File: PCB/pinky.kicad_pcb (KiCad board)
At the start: 2 copper layers, 134.3 x 87.6 mm, 50 parts, among them SW10 Switch, SW11 Switch, SW12 Switch, SW13 Switch, SW14 Switch, SW15 Switch, SW16 Switch, SW17 Switch, SW18 Switch, SW2 Switch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

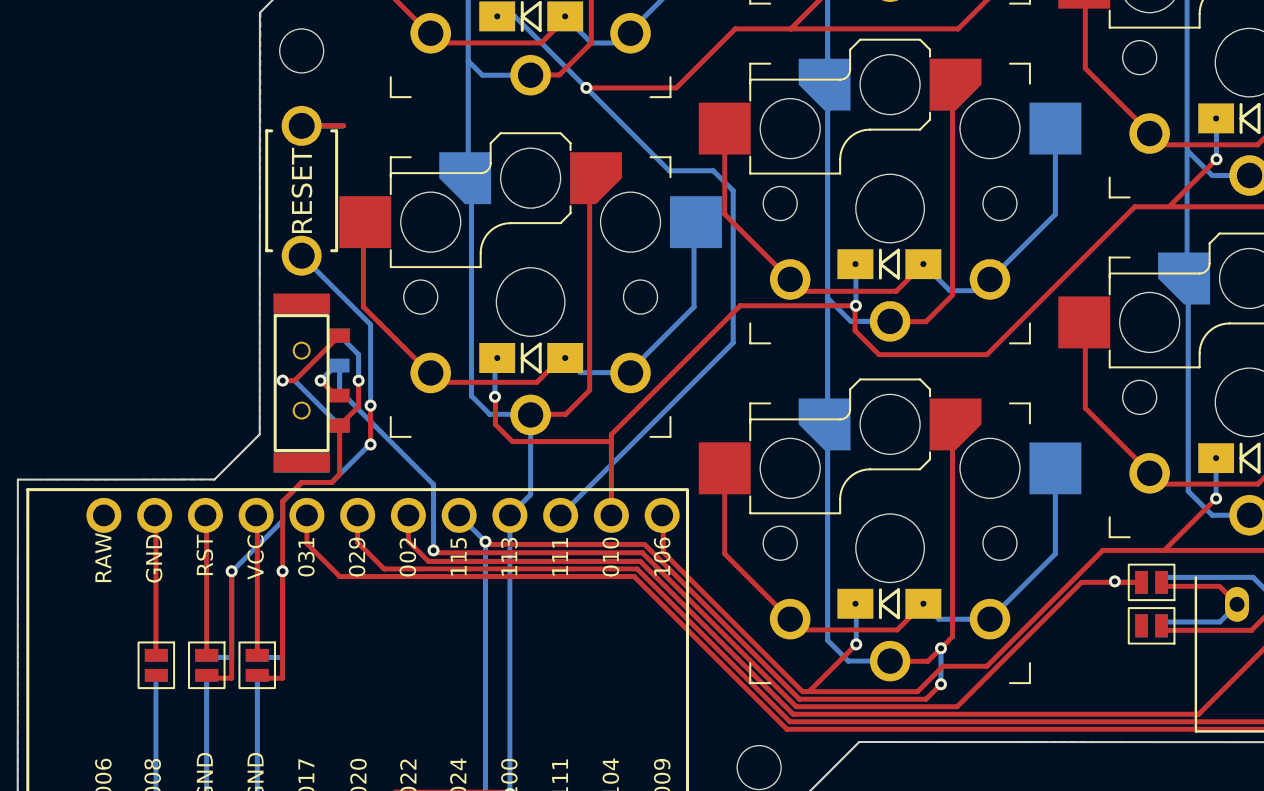
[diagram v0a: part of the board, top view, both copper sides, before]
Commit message: Added few explicit, stitching, vias to the GND fill
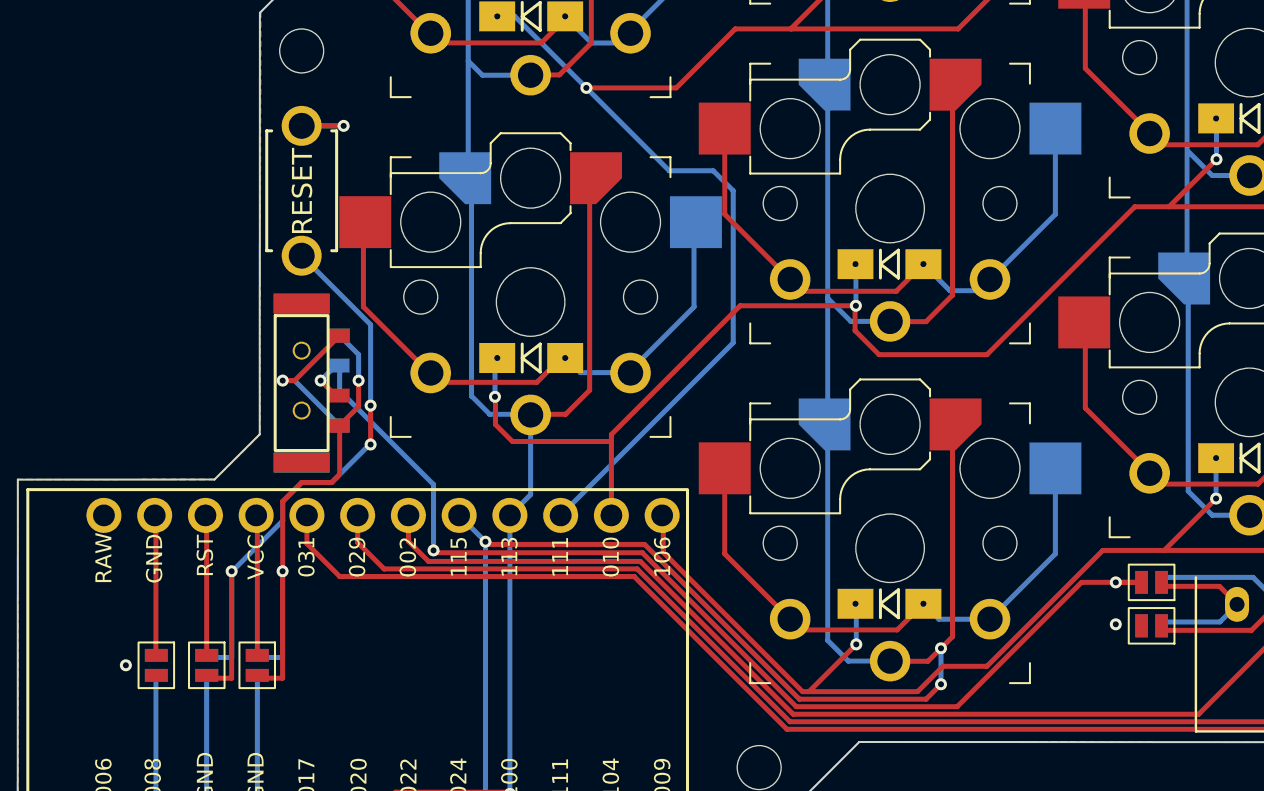
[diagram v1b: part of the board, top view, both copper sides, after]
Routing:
- net GND: vias 0 -> 3
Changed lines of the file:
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@@
+	)
+	(segment
+		(start 122.55055 100.116866)
+		(end 112.216866 100.116866)
+		(width 0.25)
+		(layer "F.Cu")
+		(net "Net-(SW_PWR1-B)")
+	)
+	(segment
+		(start 146.25 101.6)
+		(end 144.533158 101.6)
+		(width 0.25)
+		(layer "F.Cu")
+		(net "Net-(SW_PWR1-B)")
+	)
+	(segment
+		(start 138.310158 107.823)
+		(end 130.256684 107.823)
+		(width 0.25)
+		(layer "F.Cu")
+		(net "Net-(SW_PWR1-B)")
+	)
+	(segment
+		(start 144.533158 101.6)
+		(end 138.310158 107.823)
+		(width 0.25)
+		(layer "F.Cu")
+		(net "Net-(SW_PWR1-B)")
+	)
+	(segment
+		(start 146.25 101.6)
+		(end 147.541878 101.6)
+		(width 0.25)
+		(layer "F.Cu")
+		(net "Net-(SW_PWR1-B)")
+	)
+	(segment
+		(start 107.2 92.25)
+		(end 106.45 91.5)
+		(width 0.25)
+		(layer "F.Cu")
+		(net "Net-(SW_PWR1-B)")
 	)
 	(segment
@@
 		(net "Net-(SW_PWR1-B)")
 	)
-	(segment
-		(start 138.310158 107.823)
-		(end 130.256684 107.823)
-		(width 0.25)
-		(layer "F.Cu")
-		(net "Net-(SW_PWR1-B)")
-	)
-	(segment
-		(start 147.541878 101.6)
-		(end 146.25 101.6)
-		(width 0.25)
-		(layer "F.Cu")
-		(net "Net-(SW_PWR1-B)")
-	)
-	(segment
-		(start 144.533158 101.6)
-		(end 138.310158 107.823)
-		(width 0.25)
-		(layer "F.Cu")
-		(net "Net-(SW_PWR1-B)")
-	)
-	(segment
-		(start 146.2 101.55)
-		(end 146.15 101.6)
-		(width 0.25)
-		(layer "F.Cu")
-		(net "Net-(SW_PWR1-B)")
-	)
-	(segment
-		(start 146.25 101.6)
-		(end 146.2 101.55)
-		(width 0.25)
-		(layer "F.Cu")
-		(net "Net-(SW_PWR1-B)")
-	)
-	(segment
-		(start 107.2 92.25)
-		(end 106.45 91.5)
-		(width 0.25)
-		(layer "F.Cu")
-		(net "Net-(SW_PWR1-B)")
-	)
-	(segment
-		(start 146.15 101.6)
-		(end 144.533158 101.6)
-		(width 0.25)
-		(layer "F.Cu")
-		(net "Net-(SW_PWR1-B)")
-	)
-	(segment
-		(start 122.55055 100.116866)
-		(end 112.216866 100.116866)
-		(width 0.25)
-		(layer "F.Cu")
-		(net "Net-(SW_PWR1-B)")
-	)
 	(via
-		(at 146.2 101.55)
+		(at 146.25 101.6)
 		(size 0.6)
 		(drill 0.3)
@@
 	(segment
 		(start 146.25 101.6)
-		(end 146.2 101.55)
+		(end 147.541878 101.6)
 		(width 0.25)
 		(layer "B.Cu")
@@
 		(start 107.4 92)
 		(end 107.4 90.75)
-		(width 0.25)
-		(layer "B.Cu")
-		(net "Net-(SW_PWR1-B)")
-	)
-	(segment
-		(start 147.541878 101.6)
-		(end 146.25 101.6)
 		(width 0.25)
 		(layer "B.Cu")
@@
 		(net "GND")
 	)
+	(via
+		(at 107.6 78.75)
+		(size 0.6)
+		(drill 0.3)
+		(layers "F.Cu" "B.Cu")
+		(net "GND")
+	)
+	(via
+		(at 96.7 105.749805)
+		(size 0.6)
+		(drill 0.3)
+		(layers "F.Cu" "B.Cu")
+		(free yes)
+		(net "GND")
+	)
+	(via
+		(at 146.25 103.7)
+		(size 0.6)
+		(drill 0.3)
+		(layers "F.Cu" "B.Cu")
+		(free yes)
+		(net "GND")
+	)
